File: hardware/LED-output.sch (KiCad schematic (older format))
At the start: 4 parts, among them J3 Screw_Terminal_01x02, U4 HT7K1201

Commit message: Layout v1.0
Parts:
- U4: symbol homebrew:HT7K1201 -> twinkle-led-controller-rescue:HT7K1201-homebrew
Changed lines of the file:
@@
 $Descr A4 11693 8268
 encoding utf-8
-Sheet 2 11
+Sheet 10 11
 Title ""
 Date ""
@@
 $EndDescr
 $Comp
-L homebrew:HT7K1201 U4
+L twinkle-led-controller-rescue:HT7K1201-homebrew U4
 U 1 1 5F5EEE19
 P 2600 1800
@@
 AR Path="/5F6A41BA/5F5EEE19" Ref="U12"  Part="1"
 AR Path="/5F6A41C2/5F5EEE19" Ref="U13"  Part="1"
-F 0 "U4" H 2300 2100 50  0000 C CNN
+AR Path="/5F5EEE19" Ref="U12"  Part="1"
+F 0 "U13" H 2300 2100 50  0000 C CNN
 F 1 "HT7K1201" H 2850 2100 50  0000 C CNN
 F 2 "Package_TO_SOT_SMD:SOT-23-6" H 2150 1450 50  0001 C CNN
@@
 AR Path="/5F6A41BA/5F5EEE1F" Ref="J11"  Part="1"
 AR Path="/5F6A41C2/5F5EEE1F" Ref="J12"  Part="1"
-F 0 "J3" H 3830 1742 50  0000 L CNN
+F 0 "J12" H 3830 1742 50  0000 L CNN
 F 1 "Screw_Terminal_01x02" H 3500 1550 50  0000 L CNN
 F 2 "homebrew:Wurth_ScrewTerminal_1x02_P5.00mm_691137710002" H 3750 1750 50  0001 C CNN
@@
 AR Path="/5F6A41BA/5F5EEE28" Ref="#PWR048"  Part="1"
 AR Path="/5F6A41C2/5F5EEE28" Ref="#PWR051"  Part="1"
-F 0 "#PWR0102" H 2600 2000 50  0001 C CNN
+F 0 "#PWR051" H 2600 2000 50  0001 C CNN
 F 1 "GND" H 2605 2077 50  0000 C CNN
 F 2 "" H 2600 2250 50  0001 C CNN
@@
 AR Path="/5F6A41BA/5F5EEE31" Ref="C16"  Part="1"
 AR Path="/5F6A41C2/5F5EEE31" Ref="C17"  Part="1"
-F 0 "C8" H 1515 1596 50  0000 L CNN
+F 0 "C17" H 1515 1596 50  0000 L CNN
 F 1 "0.1uF" H 1515 1505 50  0000 L CNN
 F 2 "Capacitor_SMD:C_0402_1005Metric" H 1438 1400 50  0001 C CNN
@@
 AR Path="/5F6A41BA/5F5EEE38" Ref="#PWR046"  Part="1"
 AR Path="/5F6A41C2/5F5EEE38" Ref="#PWR049"  Part="1"
-F 0 "#PWR0111" H 1400 1450 50  0001 C CNN
+F 0 "#PWR049" H 1400 1450 50  0001 C CNN
 F 1 "GND" H 1405 1527 50  0000 C CNN
 F 2 "" H 1400 1700 50  0001 C CNN
@@
 AR Path="/5F6A41BA/5F5EEE3F" Ref="#PWR047"  Part="1"
 AR Path="/5F6A41C2/5F5EEE3F" Ref="#PWR050"  Part="1"
-F 0 "#PWR0112" H 2600 1200 50  0001 C CNN
+F 0 "#PWR050" H 2600 1200 50  0001 C CNN
 F 1 "+5V" H 2700 1450 50  0000 C CNN
 F 2 "" H 2600 1350 50  0001 C CNN
@@
 AR Path="/5F6A41BA/5F5EEE47" Ref="R12"  Part="1"
 AR Path="/5F6A41C2/5F5EEE47" Ref="R13"  Part="1"
-F 0 "R4" V 3143 1750 50  0000 C CNN
+F 0 "R13" V 3143 1750 50  0000 C CNN
 F 1 "180" V 3234 1750 50  0000 C CNN
 F 2 "Resistor_SMD:R_1206_3216Metric" V 3280 1750 50  0001 C CNN

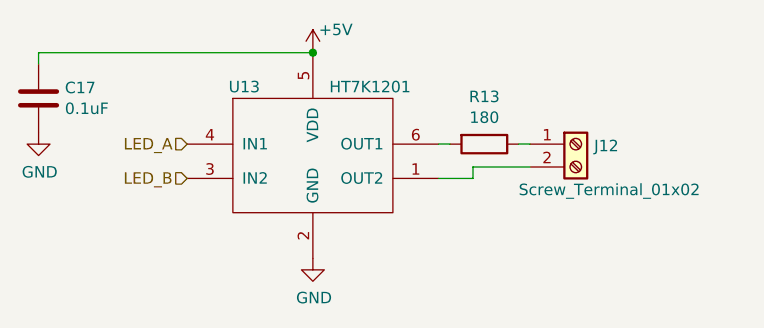
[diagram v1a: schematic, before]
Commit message: Fix v1.0 layout and generate gerbers/placement files
- Update to CP2102, since JLCPCB doesn't have CP2104
- Fix current-limiting resistors to 10 ohm
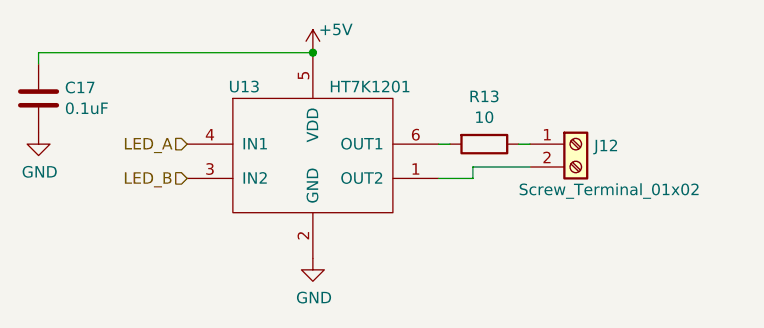
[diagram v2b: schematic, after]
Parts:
- R4: value 180 -> 10; LCSC C17924 -> C17903
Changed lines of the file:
@@
 $Descr A4 11693 8268
 encoding utf-8
-Sheet 10 11
+Sheet 2 11
 Title ""
 Date ""
@@
 AR Path="/5F6A41C2/5F5EEE47" Ref="R13"  Part="1"
 F 0 "R13" V 3143 1750 50  0000 C CNN
-F 1 "180" V 3234 1750 50  0000 C CNN
+F 1 "10" V 3234 1750 50  0000 C CNN
 F 2 "Resistor_SMD:R_1206_3216Metric" V 3280 1750 50  0001 C CNN
 F 3 "~" H 3350 1750 50  0001 C CNN
-F 4 "C17924" V 3350 1750 50  0001 C CNN "LCSC"
+F 4 "C17903" V 3350 1750 50  0001 C CNN "LCSC"
 	1    3350 1750
 	0    1    1    0

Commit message: Hardware revision 1.1:
- Fix pins to not use flash pins
- Fix screw terminal footprint (holes were too small)
- Add screw terminal for power
- Add out for multi-unit synchronization
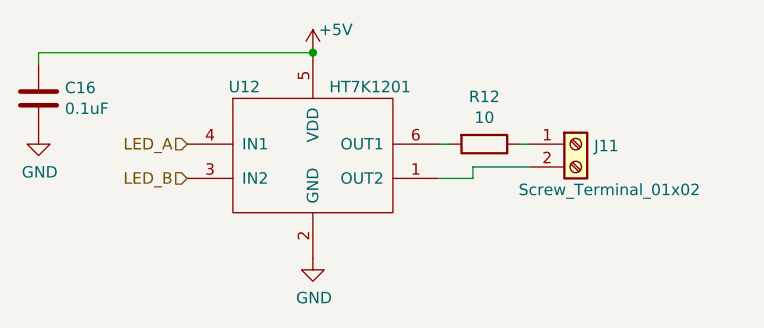
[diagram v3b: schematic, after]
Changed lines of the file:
@@
 $Descr A4 11693 8268
 encoding utf-8
-Sheet 2 11
+Sheet 2 10
 Title ""
 Date ""
@@
 AR Path="/5F6A41C2/5F5EEE19" Ref="U13"  Part="1"
 AR Path="/5F5EEE19" Ref="U12"  Part="1"
-F 0 "U13" H 2300 2100 50  0000 C CNN
+F 0 "U12" H 2300 2100 50  0000 C CNN
 F 1 "HT7K1201" H 2850 2100 50  0000 C CNN
 F 2 "Package_TO_SOT_SMD:SOT-23-6" H 2150 1450 50  0001 C CNN
@@
 AR Path="/5F6A41BA/5F5EEE1F" Ref="J11"  Part="1"
 AR Path="/5F6A41C2/5F5EEE1F" Ref="J12"  Part="1"
-F 0 "J12" H 3830 1742 50  0000 L CNN
+F 0 "J11" H 3830 1742 50  0000 L CNN
 F 1 "Screw_Terminal_01x02" H 3500 1550 50  0000 L CNN
 F 2 "homebrew:Wurth_ScrewTerminal_1x02_P5.00mm_691137710002" H 3750 1750 50  0001 C CNN
@@
 AR Path="/5F6A41BA/5F5EEE28" Ref="#PWR048"  Part="1"
 AR Path="/5F6A41C2/5F5EEE28" Ref="#PWR051"  Part="1"
-F 0 "#PWR051" H 2600 2000 50  0001 C CNN
+F 0 "#PWR048" H 2600 2000 50  0001 C CNN
 F 1 "GND" H 2605 2077 50  0000 C CNN
 F 2 "" H 2600 2250 50  0001 C CNN
@@
 AR Path="/5F6A41BA/5F5EEE31" Ref="C16"  Part="1"
 AR Path="/5F6A41C2/5F5EEE31" Ref="C17"  Part="1"
-F 0 "C17" H 1515 1596 50  0000 L CNN
+F 0 "C16" H 1515 1596 50  0000 L CNN
 F 1 "0.1uF" H 1515 1505 50  0000 L CNN
 F 2 "Capacitor_SMD:C_0402_1005Metric" H 1438 1400 50  0001 C CNN
@@
 AR Path="/5F6A41BA/5F5EEE38" Ref="#PWR046"  Part="1"
 AR Path="/5F6A41C2/5F5EEE38" Ref="#PWR049"  Part="1"
-F 0 "#PWR049" H 1400 1450 50  0001 C CNN
+F 0 "#PWR046" H 1400 1450 50  0001 C CNN
 F 1 "GND" H 1405 1527 50  0000 C CNN
 F 2 "" H 1400 1700 50  0001 C CNN
@@
 AR Path="/5F6A41BA/5F5EEE3F" Ref="#PWR047"  Part="1"
 AR Path="/5F6A41C2/5F5EEE3F" Ref="#PWR050"  Part="1"
-F 0 "#PWR050" H 2600 1200 50  0001 C CNN
+F 0 "#PWR047" H 2600 1200 50  0001 C CNN
 F 1 "+5V" H 2700 1450 50  0000 C CNN
 F 2 "" H 2600 1350 50  0001 C CNN
@@
 AR Path="/5F6A41BA/5F5EEE47" Ref="R12"  Part="1"
 AR Path="/5F6A41C2/5F5EEE47" Ref="R13"  Part="1"
-F 0 "R13" V 3143 1750 50  0000 C CNN
+F 0 "R12" V 3143 1750 50  0000 C CNN
 F 1 "10" V 3234 1750 50  0000 C CNN
 F 2 "Resistor_SMD:R_1206_3216Metric" V 3280 1750 50  0001 C CNN
